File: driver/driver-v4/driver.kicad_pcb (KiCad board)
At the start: 2 copper layers, 80.5 x 25 mm, 16 parts, among them J1 Conn_01x05, J2 Conn_01x05, J3 Conn_01x08_Pin, J4 Conn_01x08_Socket, U1 GR2803LSS24ARCQ, U2 74HC595D,118, U3 DRV5032DGDMRR, U4 DRV5032DGDMRR, U5 SN74HC165DR(LX)

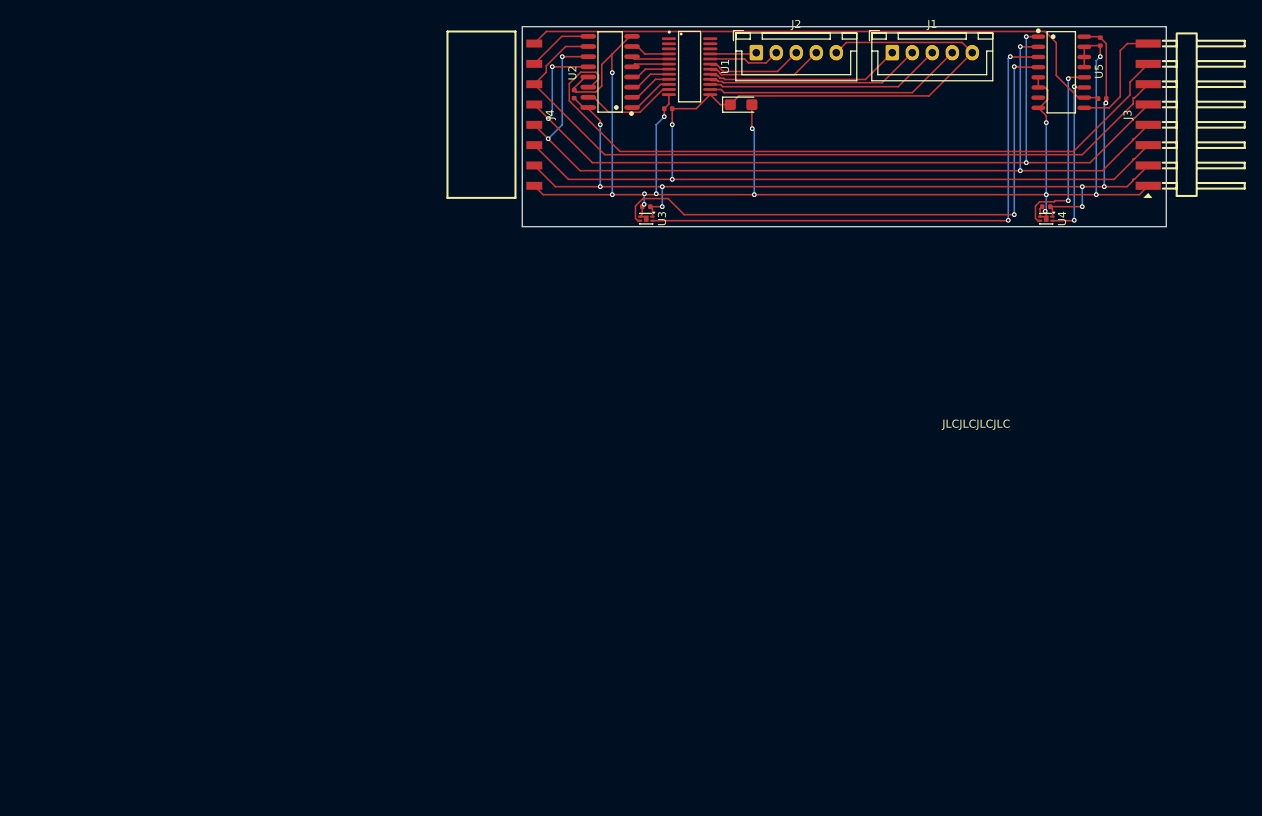
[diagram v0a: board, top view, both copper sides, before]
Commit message: Added surface mount connectors.
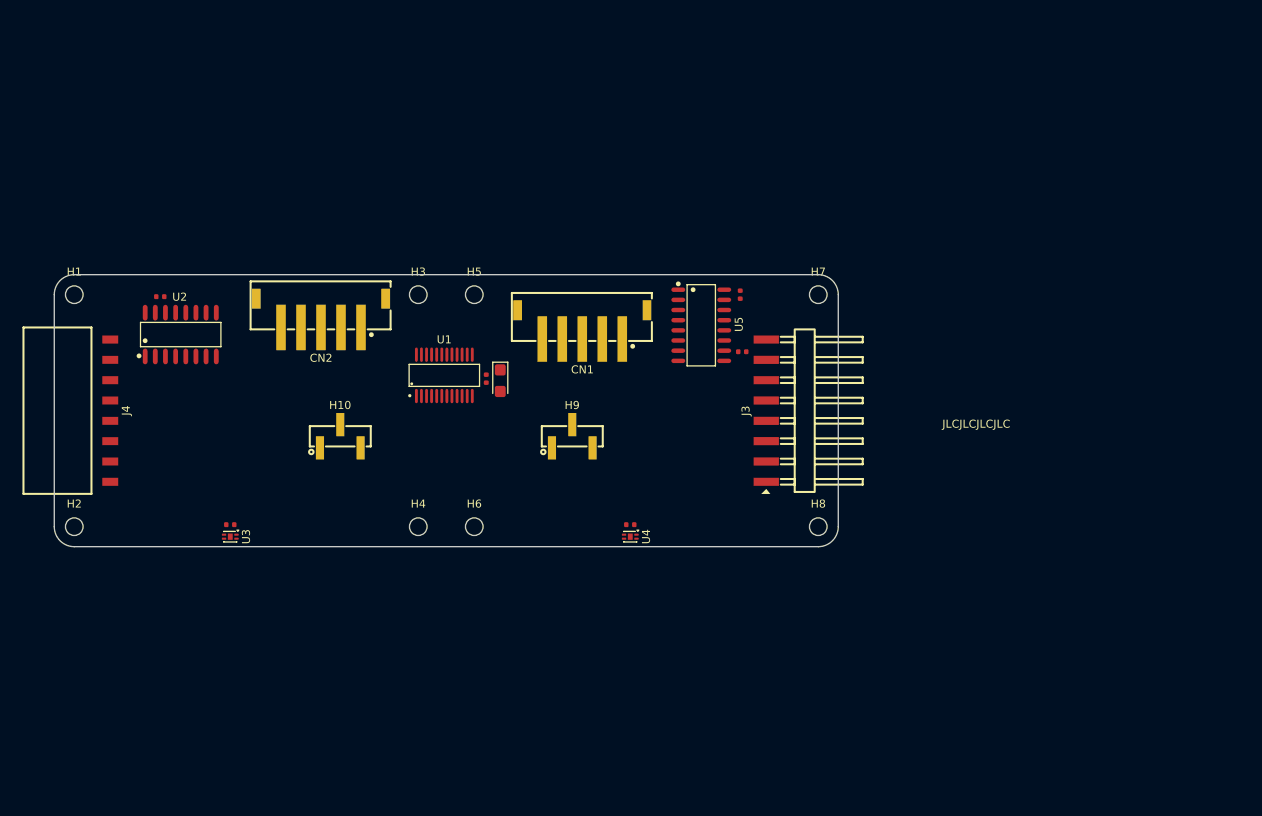
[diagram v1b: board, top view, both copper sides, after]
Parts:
- removed J1, J2: Conn_01x05, Connector_JST:JST_XH_B5B-XH-A_1x05_P2.50mm_Vertical
- added CN1: ~, CONN-SMD_5P-P2.50_2.54-5P-LT:CONN-SMD_5P-P2.50_2.54-5P-LT, F.Cu at (117.0, 57.2)
- added CN2: ~, CONN-SMD_5P-P2.50_2.54-5P-LT:CONN-SMD_5P-P2.50_2.54-5P-LT, F.Cu at (84.3, 55.8)
- added H1: MountingHole, MountingHole:MountingHole_2.2mm_M2_ISO14580, F.Cu at (53.5, 53.5)
- added H10: ~, HDR-TH_3P-P2.54_DZ254S-11-03-48:HDR-TH_3P-P2.54_DZ254S-11-03-48, F.Cu at (86.8, 71.2)
- added H2: MountingHole, MountingHole:MountingHole_2.2mm_M2_ISO14580, F.Cu at (53.5, 82.5)
- added H3: MountingHole, MountingHole:MountingHole_2.2mm_M2_ISO14580, F.Cu at (96.5, 53.5)
- added H4: MountingHole, MountingHole:MountingHole_2.2mm_M2_ISO14580, F.Cu at (96.5, 82.5)
- added H5: MountingHole, MountingHole:MountingHole_2.2mm_M2_ISO14580, F.Cu at (103.5, 53.5)
- added H6: MountingHole, MountingHole:MountingHole_2.2mm_M2_ISO14580, F.Cu at (103.5, 82.5)
- added H7: MountingHole, MountingHole:MountingHole_2.2mm_M2_ISO14580, F.Cu at (146.5, 53.5)
- added H8: MountingHole, MountingHole:MountingHole_2.2mm_M2_ISO14580, F.Cu at (146.5, 82.5)
- added H9: ~, HDR-TH_3P-P2.54_DZ254S-11-03-48:HDR-TH_3P-P2.54_DZ254S-11-03-48, F.Cu at (115.8, 71.2)
- moved C1 65.5 mm to (73.0, 82.2)
- moved C2 65.5 mm to (123.0, 82.2)
- moved U3 65.5 mm to (73.0, 83.8)
- moved U4 65.5 mm to (123.0, 83.8)
- moved J4 64.6 mm to (58.0, 68.0)
- moved U2 62.9 mm to (66.8, 58.5), turned to 0 degrees
- moved J3 60.4 mm to (140.0, 68.0)
- moved C4 57.6 mm to (64.2, 53.8), turned to 0 degrees
- moved C3 55.0 mm to (136.7, 53.5)
- moved R1 55.0 mm to (137.0, 60.6)
- moved U5 55.0 mm to (131.9, 57.3)
- moved U1 49.3 mm to (99.8, 63.6), turned to 0 degrees
- moved C6 45.8 mm to (106.8, 64.2), turned to -90 degrees
- moved C5 40.7 mm to (105.0, 64.0), turned to -90 degrees
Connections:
- U5 pad 13: GND -> Net-(U5-D2)
- U5 pad 5: GND -> Net-(U5-D6)
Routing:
- net GND: track 183.4 -> 0.00 mm, vias 13 -> 0
- net +12V: track 148.7 -> 0.00 mm, vias 2 -> 0
- net +3V3: track 126.1 -> 0.00 mm, vias 8 -> 0
- net SCLK: track 113.6 -> 0.00 mm, vias 4 -> 0
- net LATCH: track 111.3 -> 0.00 mm, vias 4 -> 0
- net RESET: track 93.6 -> 0.00 mm
- net COPI1: track 89.2 -> 0.00 mm
- net CIPO2: track 77.0 -> 0.00 mm
- net Net-(U3-OUT2): track 72.3 -> 0.00 mm, vias 2 -> 0
- net Net-(U3-OUT1): track 68.6 -> 0.00 mm, vias 2 -> 0
- net Net-(U1-8C): track 32.5 -> 0.00 mm
- net Net-(U1-7C): track 29.6 -> 0.00 mm
- net Net-(U1-6C): track 27.0 -> 0.00 mm
- net Net-(U1-5C): track 24.4 -> 0.00 mm
- net Net-(U4-OUT2): track 23.9 -> 0.00 mm, vias 2 -> 0
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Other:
- board size 80.5 x 25 mm -> 98 x 34 mm

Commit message: Fix missing part on JLC.
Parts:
- CN1, CN2: value ~ -> Conn_01x05_Pin
- H10, H9: value ~ -> Conn_01x03_Pin
- J4: value Conn_01x08_Socket -> X6511FRS-08-C85D30; footprint HX PM2.54-1x8P WT:HDR-SMD_8P-P2.54-H-F-W8.5 -> HDR-SMD_8P-P2.54-H-F-L11.5:HDR-SMD_8P-P2.54-H-F-L11.5
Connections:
- J3 pad 1: GND -> CIPO1
- J3 pad 2: +3V3 -> COPI1
- J3 pad 3: +12V -> RESET
- J3 pad 4: SCLK -> LATCH
- J3 pad 5: LATCH -> SCLK
- J3 pad 6: RESET -> +12V
- J3 pad 7: COPI1 -> +3V3
- J3 pad 8: CIPO1 -> GND
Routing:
- added copper zone on F.Cu, net +12V
- added copper zone on B.Cu, net +3V3
- added copper zone on In1.Cu, net GND
- added copper zone on In2.Cu, net GND
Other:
- copper layers 2 -> 4

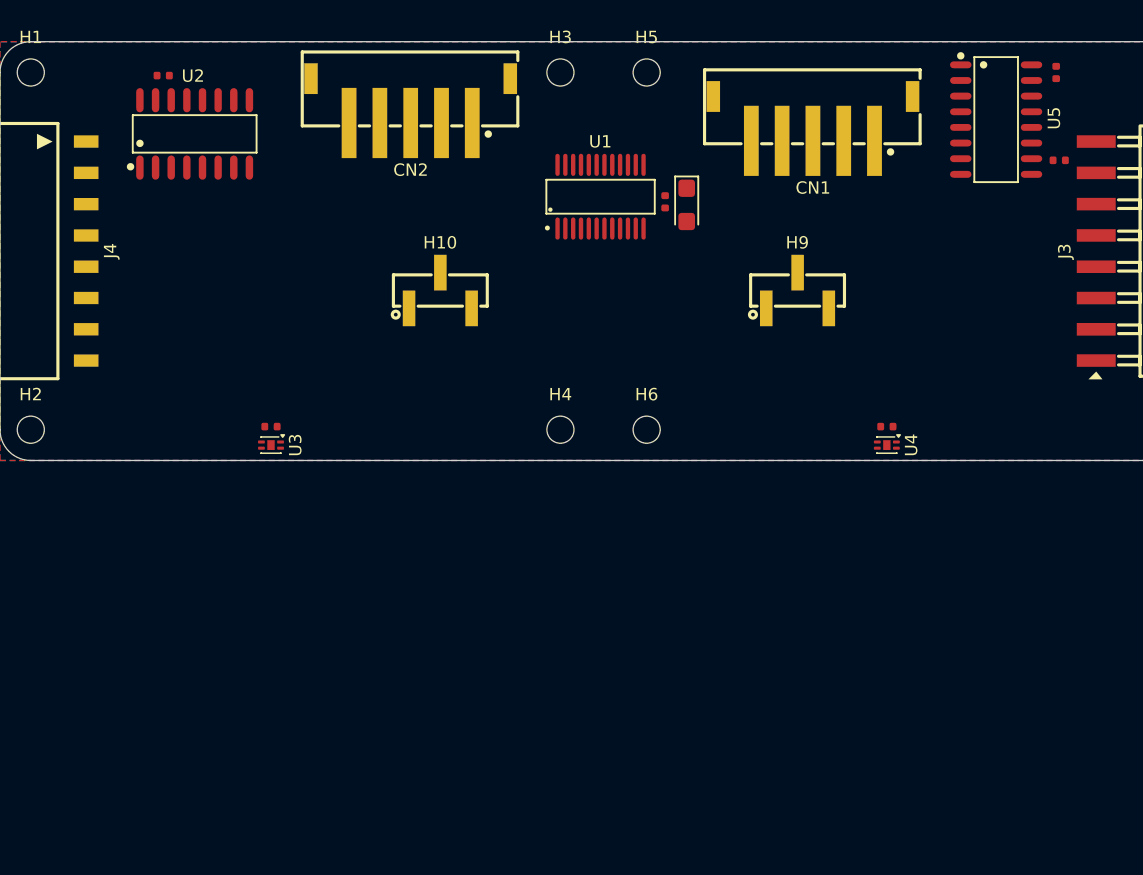
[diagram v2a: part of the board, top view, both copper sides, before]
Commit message: Start laying traces.
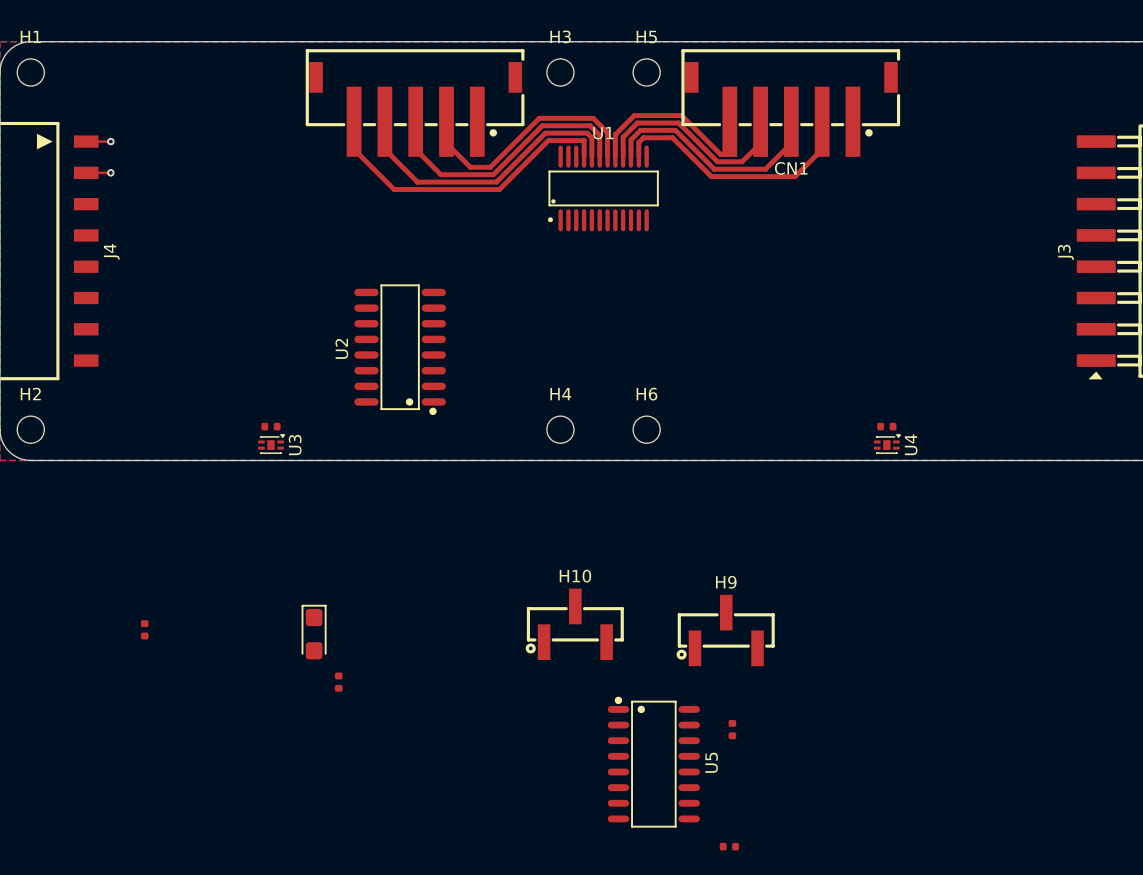
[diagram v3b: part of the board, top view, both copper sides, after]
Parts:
- moved R1 61.8 mm to (110.2, 116.3)
- moved C3 59.5 mm to (110.5, 106.8)
- moved U5 59.3 mm to (104.1, 109.7)
- moved C5 47.2 mm to (78.5, 103.0)
- moved C6 46.1 mm to (76.5, 99.1)
- moved C4 45.0 mm to (62.8, 98.8), turned to 90 degrees
- moved H10 29.2 mm to (97.7, 98.3)
- moved H9 28.2 mm to (110.0, 98.8)
- moved U2 24.0 mm to (83.5, 75.8), turned to 90 degrees
- moved CN1 2.34 mm to (115.2, 55.7)
- moved U1 0.72 mm to (100.0, 62.9)
- moved CN2 0.42 mm to (84.8, 55.7)
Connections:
- net Net-(U1-1C) renamed PB4
- net Net-(U1-2C) renamed PB3
- net Net-(U1-3C) renamed PB2
- net Net-(U1-4C) renamed PB1
- net Net-(U1-5C) renamed PA4
- net Net-(U1-6C) renamed PA3
- net Net-(U1-7C) renamed PA2
- net Net-(U1-8C) renamed PA1
- CN1 pad 6: unconnected-(CN1-Pad6) -> +12V
- CN1 pad 7: unconnected-(CN1-Pad7) -> +12V
- CN2 pad 6: unconnected-(CN2-Pad6) -> +12V
- CN2 pad 7: unconnected-(CN2-Pad7) -> +12V
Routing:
- net PB4: track 0.00 -> 25.2 mm
- net PB3: track 0.00 -> 23.5 mm
- net PB2: track 0.00 -> 21.7 mm
- net PA1: track 0.00 -> 20.7 mm
- net PB1: track 0.00 -> 19.7 mm
- net PA2: track 0.00 -> 18.6 mm
- net PA3: track 0.00 -> 16.9 mm
- net PA4: track 0.00 -> 15.7 mm
- net GND: track 0.00 -> 2.00 mm, vias 0 -> 1
- net +3V3: track 0.00 -> 2.00 mm, vias 0 -> 1

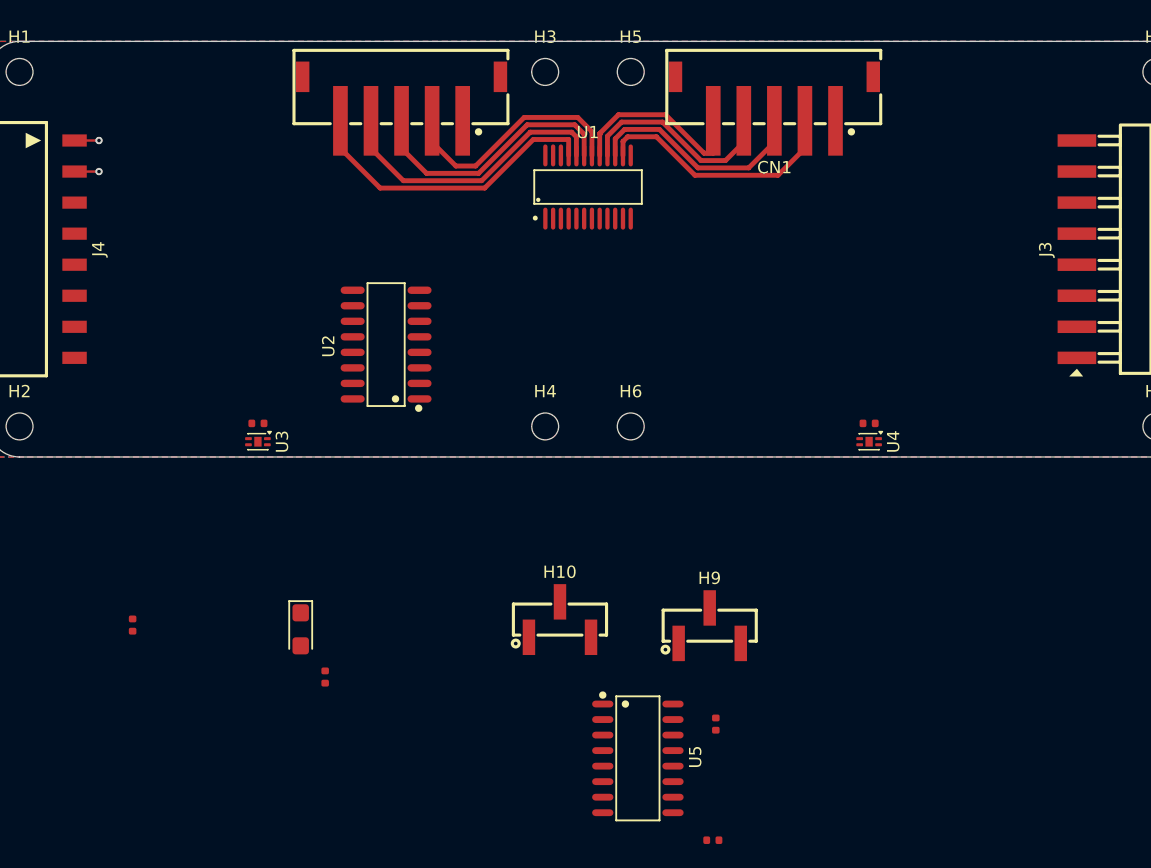
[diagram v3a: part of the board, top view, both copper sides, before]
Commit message: Completed initial traces.
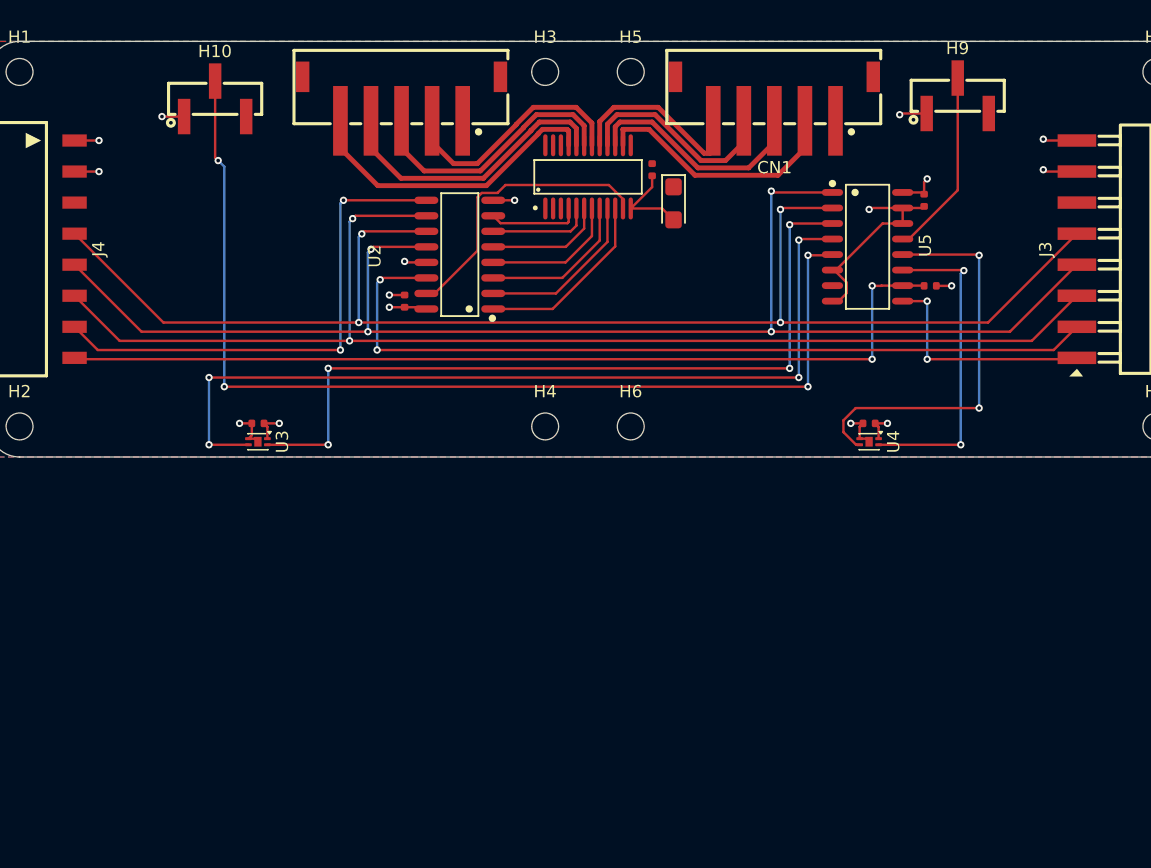
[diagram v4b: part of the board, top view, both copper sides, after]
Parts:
- moved H10 51.1 mm to (69.5, 55.7)
- moved C5 49.4 mm to (105.2, 61.5)
- moved R1 48.7 mm to (128.0, 71.0)
- moved H9 47.9 mm to (130.2, 55.5)
- moved C6 46.3 mm to (107.0, 64.2)
- moved C3 46.1 mm to (127.5, 64.0)
- moved U5 45.9 mm to (122.9, 67.8)
- moved C4 34.6 mm to (85.0, 72.2)
- moved U2 9.51 mm to (89.5, 68.4)
- moved U1 0.83 mm to (100.0, 62.1)
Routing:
- net LATCH: track 0.00 -> 114.5 mm, vias 0 -> 4
- net SCLK: track 0.00 -> 114.3 mm, vias 0 -> 4
- net RESET: track 0.00 -> 101.3 mm, vias 0 -> 2
- net Net-(U5-D6): track 0.00 -> 85.8 mm, vias 0 -> 4
- net CIPO2: track 0.00 -> 75.6 mm, vias 0 -> 2
- net Net-(U3-OUT2): track 0.00 -> 71.0 mm, vias 0 -> 4
- net COPI1: track 0.00 -> 67.7 mm, vias 0 -> 2
- net Net-(U3-OUT1): track 0.00 -> 64.3 mm, vias 0 -> 4
- net GND: track 2.00 -> 44.5 mm, vias 1 -> 10
- net COPI2: track 0.00 -> 41.7 mm, vias 0 -> 2
- net Net-(U4-OUT2): track 0.00 -> 33.0 mm, vias 0 -> 2
- net Net-(U4-OUT1): track 0.00 -> 26.1 mm, vias 0 -> 2
- net MA1: track 0.00 -> 23.6 mm
- net CIPO1: track 0.00 -> 19.1 mm, vias 0 -> 2
- net Net-(U5-D2): track 0.00 -> 15.3 mm
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
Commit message: Use continuous hall sensors, add silkscreen logo, and order signal lines in line with MCU.
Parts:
- added G1: LOGO, BurntOutBakery:BurntOutBakery, F.Cu at (84.5, 76.2)
- added R10: 10kΩ, PCM_JLCPCB:R_0402, F.Cu at (70.8, 81.5)
- added R11: 10kΩ, PCM_JLCPCB:R_0402, F.Cu at (120.5, 81.5)
- added R12: 10kΩ, PCM_JLCPCB:R_0402, F.Cu at (69.5, 54.0)
- added R13: 10kΩ, PCM_JLCPCB:R_0402, F.Cu at (135.0, 54.5)
- added R2: 10kΩ, PCM_JLCPCB:R_0402, F.Cu at (81.5, 65.8)
- added R3: 10kΩ, PCM_JLCPCB:R_0402, F.Cu at (84.8, 67.0)
- added R4: 10kΩ, PCM_JLCPCB:R_0402, F.Cu at (88.8, 68.2)
- added R5: 10kΩ, PCM_JLCPCB:R_0402, F.Cu at (92.2, 69.5)
- added R6: 10kΩ, PCM_JLCPCB:R_0402, F.Cu at (95.8, 70.8)
- added R7: 10kΩ, PCM_JLCPCB:R_0402, F.Cu at (99.5, 72.0)
- added R8: 10kΩ, PCM_JLCPCB:R_0402, F.Cu at (102.8, 73.0)
- added R9: 10kΩ, PCM_JLCPCB:R_0402, F.Cu at (77.6, 64.5)
- U3, U4: value DRV5032DGDMRR -> MT3151AT-EN; footprint Package_SON:Texas_X2SON-4-1EP_1.1x1.4mm_P0.5mm_EP0.8x0.6mm -> SOT-23-3_L2.9-W1.3-P1.90-LS2.4-BR:SOT-23-3_L2.9-W1.3-P1.90-LS2.4-BR
- moved C4 19.3 mm to (65.7, 70.6)
- moved U2 19.3 mm to (70.2, 66.8)
- moved H10 4.87 mm to (64.7, 54.8)
- moved C1 1.75 mm to (73.0, 80.5)
- moved C2 1.75 mm to (123.0, 80.5)
- moved U3 0.79 mm to (73.2, 83.0), turned to 90 degrees
- moved U4 0.79 mm to (122.8, 83.0), turned to 90 degrees
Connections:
- C1 pad 1: +3V3 -> +12V
- C2 pad 1: +3V3 -> +12V
- H10 pad 2: Net-(U5-D6) -> SEB
- H9 pad 2: Net-(U5-D2) -> SEA
- J3 pad 1: CIPO1 -> ENABLE
- J3 pad 3: RESET -> SCLK
- J3 pad 5: SCLK -> CIPO1
- J4 pad 4: SCLK -> CIPO2
- J4 pad 6: RESET -> SCLK
- J4 pad 8: CIPO2 -> ENABLE
- U2 pad 10: RESET -> +3V3
- U2 pad 13: GND -> ENABLE
- U3 pad 1: +3V3 -> +12V
- U3 pad 2: GND -> SIB
- U3 pad 3: Net-(U3-OUT2) -> GND
- U4 pad 1: +3V3 -> +12V
- U4 pad 2: GND -> SIA
- U4 pad 3: Net-(U4-OUT2) -> GND
- U5 pad 11: Net-(U4-OUT1) -> SIA
- U5 pad 12: Net-(U4-OUT2) -> SEA
- U5 pad 13: Net-(U5-D2) -> GND
- U5 pad 3: Net-(U3-OUT1) -> SIB
- U5 pad 4: Net-(U3-OUT2) -> SEB
- U5 pad 5: Net-(U5-D6) -> GND
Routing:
- net RESET: track 101.3 -> 0.00 mm, vias 2 -> 0
- net ENABLE: track 0.00 -> 97.9 mm, vias 0 -> 2
- net SEB: track 0.00 -> 96.3 mm, vias 0 -> 4
- net Net-(U5-D6): track 85.8 -> 0.00 mm, vias 4 -> 0
- net Net-(U3-OUT2): track 71.0 -> 0.00 mm, vias 4 -> 0
- net SIB: track 0.00 -> 68.8 mm, vias 0 -> 4
- net Net-(U3-OUT1): track 64.3 -> 0.00 mm, vias 4 -> 0
- net Net-(U4-OUT2): track 33.0 -> 0.00 mm, vias 2 -> 0
- net SIA: track 0.00 -> 32.8 mm, vias 0 -> 2
- net Net-(U4-OUT1): track 26.1 -> 0.00 mm, vias 2 -> 0
- net MA1: track 23.6 -> 46.9 mm
- net MA2: track 15.2 -> 38.3 mm
- net MA3: track 13.8 -> 35.3 mm
- net SEA: track 0.00 -> 21.4 mm
- net COPI1: track 67.7 -> 88.8 mm
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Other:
- board text added: "FlappyDriver 4.0"

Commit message: Actually add test points.
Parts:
- added MA1: TestPoint, TestPoint:TestPoint_THTPad_D2.0mm_Drill1.0mm, F.Cu at (107.2, 69.2)
- added SIA1: TestPoint, TestPoint:TestPoint_THTPad_D2.0mm_Drill1.0mm, F.Cu at (118.0, 82.2)
- added SIB1: TestPoint, TestPoint:TestPoint_THTPad_D2.0mm_Drill1.0mm, F.Cu at (67.2, 82.8)
- moved J4 0.80 mm to (57.2, 68.0)
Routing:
- net MA1: track 46.9 -> 54.4 mm
- net +12V: track 1.79 -> 7.37 mm
- net LATCH: track 115.6 -> 112.8 mm
- net SIA: track 32.8 -> 35.4 mm
- net CIPO2: track 75.6 -> 73.8 mm, vias 2 -> 0
- net ENABLE: track 97.9 -> 96.3 mm
- net SEB: track 96.3 -> 94.9 mm
- net SCLK: track 112.8 -> 114.1 mm
- net CIPO1: track 19.1 -> 18.0 mm, vias 2 -> 0
- net SIB: track 68.8 -> 69.7 mm
